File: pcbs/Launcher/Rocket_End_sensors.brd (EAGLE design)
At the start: 100 x 80 mm, 9 parts, among them U1 ARDUINO-MEGAPRO-5V, X1 22-23-2051, X3 22-23-2041, X5 22-23-2101, X6 22-23-2101, X7 22-23-2101, X8 22-23-2031

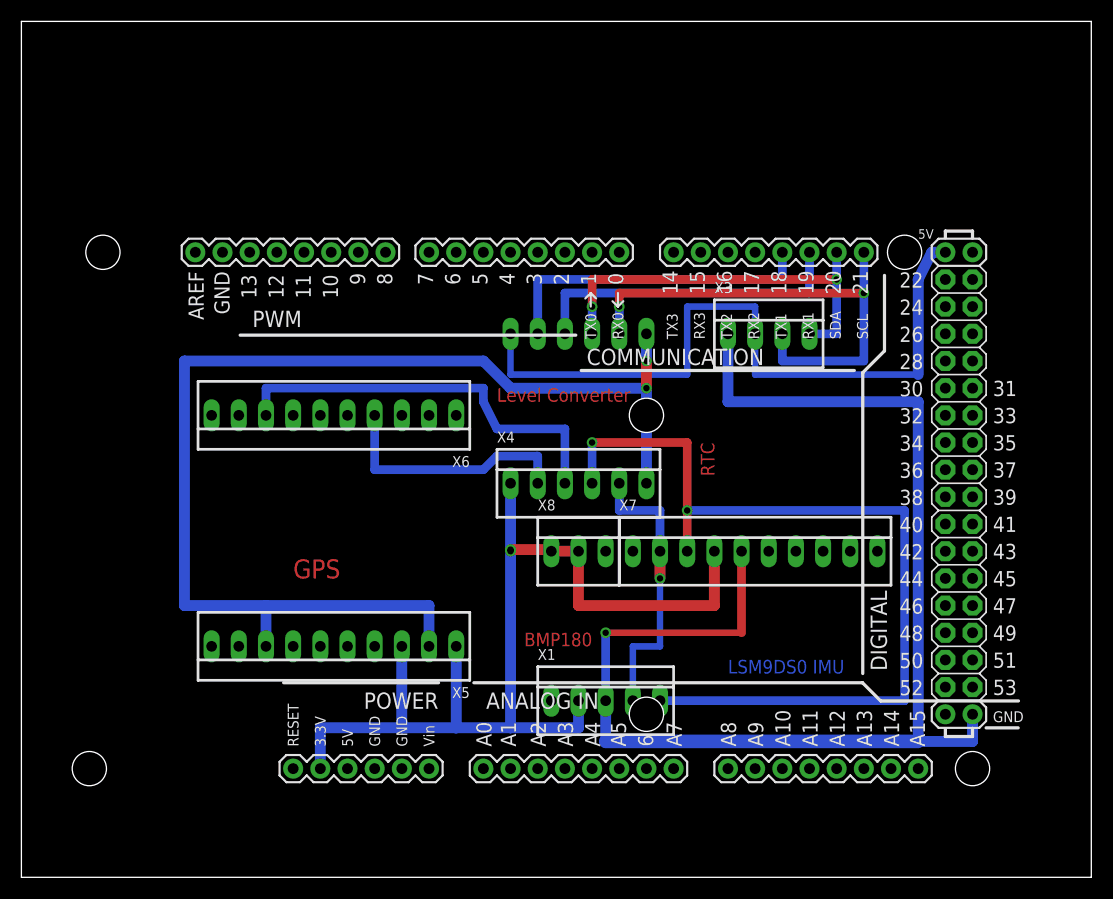
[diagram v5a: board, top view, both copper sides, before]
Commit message: * More space between tracks * Ground wire added to GPS module * Added extra holes, so we can do some hacks alter on the IMU
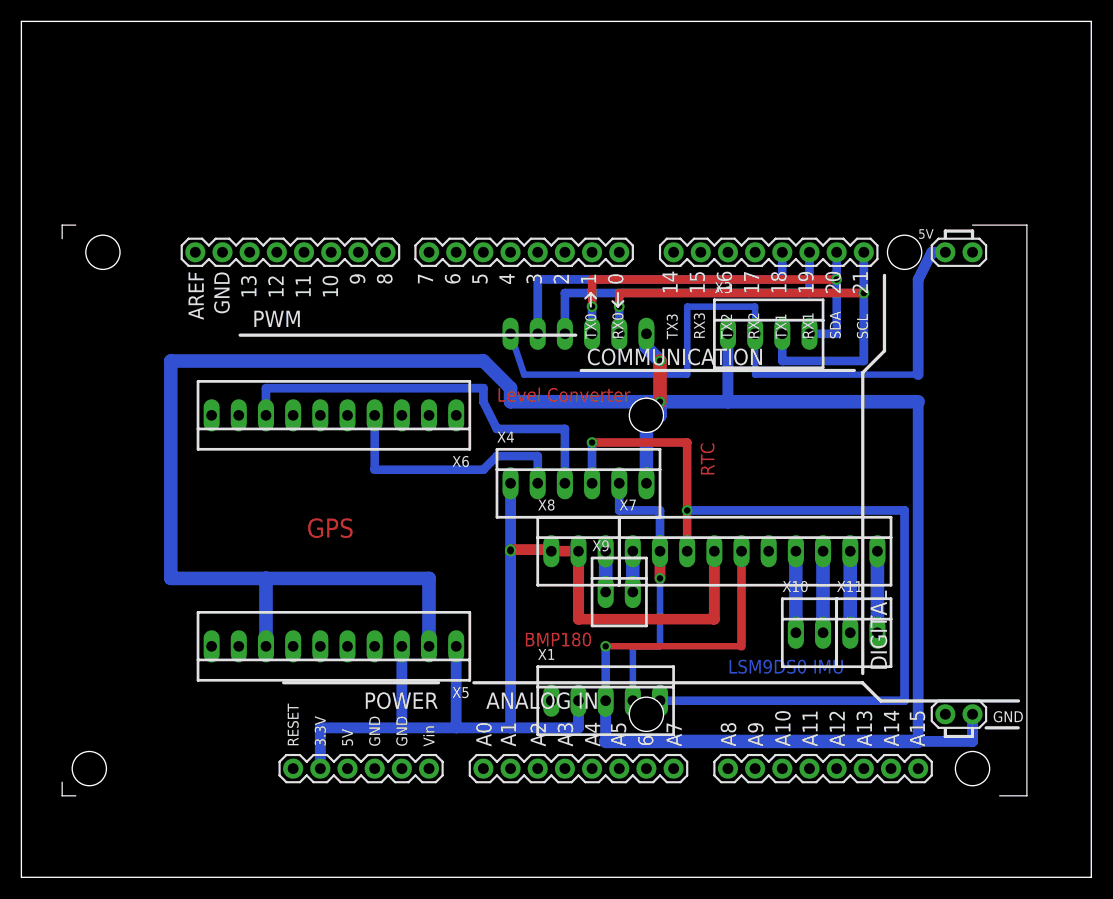
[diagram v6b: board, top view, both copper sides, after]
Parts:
- added X10, X11, X9: 22-23-2021, con-molex:22-23-2021
- U1: device SparkFun-Boards:ARDUINO_MEGA-PRO-5V -> JoeMega_Ether_Edited:ARDUINO_MEGA-PRO-5V
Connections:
- new net N$10: X10.1, X7.7
- new net N$11: X10.2, X7.8
- new net N$12: X11.1, X7.9
- new net N$13: X11.2, X7.10
- new net N$9: X7.1, X9.2
- net GND: now also X2.1, X4.6, X5.2, X5.8
- net N$7: now also X8.3, X9.1; no longer X2.1, X4.6, X5.2, X5.8
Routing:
- net GND: track 123.2 -> 248.5 mm, vias 1 -> 3
- net N$7: track 111.5 -> 3.81 mm, vias 2 -> 0
- net N$13: track 0.00 -> 7.62 mm
- net N$12: track 0.00 -> 7.62 mm
- net N$11: track 0.00 -> 7.62 mm
- net N$10: track 0.00 -> 7.62 mm
- net N$9: track 0.00 -> 3.81 mm
- net N$4: track 97.7 -> 100.2 mm
- net N$28: track 67.6 -> 66.5 mm
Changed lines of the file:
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@@
 <?xml version="1.0" encoding="utf-8"?>
 <!DOCTYPE eagle SYSTEM "eagle.dtd">
-<eagle version="7.1.0">
+<eagle version="7.3.0">
 <drawing>
 <settings>
@@
 <wire x1="0" y1="80" x2="0" y2="0" width="0" layer="20"/>
 <text x="63.5" y="40.64" size="1.27" layer="1" rot="R270">RTC</text>
-<text x="25.4" y="27.94" size="1.778" layer="1">GPS</text>
+<text x="26.67" y="31.75" size="1.778" layer="1">GPS</text>
 <text x="46.99" y="21.59" size="1.27" layer="1">BMP180</text>
 <text x="66.04" y="19.05" size="1.27" layer="16">LSM9DS0 IMU</text>
@@
 </autorouter>
 <elements>
-<element name="U1" library="SparkFun-Boards" package="ARDUINO_MEGA-PRO-5V" value="ARDUINO-MEGAPRO-5V" x="3.81" y="7.62"/>
+<element name="U1" library="JoeMega_Ether_Edited" package="ARDUINO_MEGA-PRO-5V" value="ARDUINO-MEGAPRO-5V" x="3.81" y="7.62"/>
 <element name="X3" library="con-molex" package="22-23-2041" value="22-23-2041" x="69.85" y="50.8">
 <attribute name="MF" value="MOLEX" x="69.85" y="50.8" size="1.778" layer="27" display="off"/>
@@
 <attribute name="MF" value="MOLEX" x="29.21" y="21.59" size="1.778" layer="27" rot="R180" display="off"/>
 <attribute name="OC_FARNELL" value="1756828" x="29.21" y="21.59" size="1.778" layer="27" rot="R180" display="off"/>
+</element>
+<element name="X9" library="con-molex" package="22-23-2021" value="22-23-2021" x="55.88" y="26.67">
+<attribute name="OC_FARNELL" value="1462926" x="55.88" y="26.67" size="1.778" layer="27" display="off"/>
+<attribute name="OC_NEWARK" value="25C3832" x="55.88" y="26.67" size="1.778" layer="27" display="off"/>
+<attribute name="MPN" value="22-23-2021" x="55.88" y="26.67" size="1.778" layer="27" display="off"/>
+<attribute name="MF" value="MOLEX" x="55.88" y="26.67" size="1.778" layer="27" display="off"/>
+</element>
+<element name="X10" library="con-molex" package="22-23-2021" value="22-23-2021" x="73.66" y="22.86">
+<attribute name="OC_FARNELL" value="1462926" x="73.66" y="22.86" size="1.778" layer="27" display="off"/>
+<attribute name="OC_NEWARK" value="25C3832" x="73.66" y="22.86" size="1.778" layer="27" display="off"/>
+<attribute name="MPN" value="22-23-2021" x="73.66" y="22.86" size="1.778" layer="27" display="off"/>
+<attribute name="MF" value="MOLEX" x="73.66" y="22.86" size="1.778" layer="27" display="off"/>
+</element>
+<element name="X11" library="con-molex" package="22-23-2021" value="22-23-2021" x="78.74" y="22.86">
+<attribute name="OC_FARNELL" value="1462926" x="78.74" y="22.86" size="1.778" layer="27" display="off"/>
+<attribute name="OC_NEWARK" value="25C3832" x="78.74" y="22.86" size="1.778" layer="27" display="off"/>
+<attribute name="MPN" value="22-23-2021" x="78.74" y="22.86" size="1.778" layer="27" display="off"/>
+<attribute name="MF" value="MOLEX" x="78.74" y="22.86" size="1.778" layer="27" display="off"/>
 </element>
 </elements>
@@
 <wire x1="68.58" y1="53.34" x2="62.23" y2="53.34" width="0.6096" layer="16"/>
 <wire x1="62.23" y1="53.34" x2="62.23" y2="46.99" width="0.6096" layer="16"/>
-<wire x1="62.23" y1="46.99" x2="45.72" y2="46.99" width="0.6096" layer="16"/>
-<wire x1="45.72" y1="46.99" x2="45.72" y2="50.8" width="0.6096" layer="16"/>
+<wire x1="62.23" y1="46.99" x2="46.99" y2="46.99" width="0.6096" layer="16"/>
+<wire x1="46.99" y1="46.99" x2="45.72" y2="50.8" width="0.6096" layer="16"/>
 </signal>
 <signal name="N$32">
@@
 <contactref element="U1" pad="GND@3"/>
 <wire x1="66.04" y1="50.8" x2="66.04" y2="44.45" width="1.016" layer="16"/>
-<wire x1="66.04" y1="44.45" x2="83.82" y2="44.45" width="1.016" layer="16"/>
+<wire x1="66.04" y1="44.45" x2="83.82" y2="44.45" width="1.27" layer="16"/>
 <wire x1="83.82" y1="44.45" x2="83.82" y2="12.7" width="1.016" layer="16"/>
 <wire x1="83.82" y1="12.7" x2="88.9" y2="12.7" width="1.016" layer="16"/>
@@
 <wire x1="54.61" y1="12.7" x2="83.82" y2="12.7" width="1.27" layer="16"/>
 <contactref element="X7" pad="5"/>
-<wire x1="67.31" y1="30.48" x2="67.31" y2="22.86" width="0.8128" layer="1"/>
-<wire x1="67.31" y1="22.86" x2="54.61" y2="22.86" width="0.6096" layer="1"/>
-<wire x1="54.61" y1="22.86" x2="54.61" y2="16.51" width="0.8128" layer="16"/>
-<via x="54.61" y="22.86" extent="1-16" drill="0.6" shape="square"/>
+<wire x1="67.31" y1="30.48" x2="67.31" y2="21.59" width="0.8128" layer="1"/>
+<wire x1="67.31" y1="21.59" x2="54.61" y2="21.59" width="0.6096" layer="1"/>
+<wire x1="54.61" y1="21.59" x2="54.61" y2="16.51" width="0.8128" layer="16"/>
+<via x="54.61" y="21.59" extent="1-16" drill="0.6" shape="square"/>
+<contactref element="X2" pad="1"/>
+<contactref element="X5" pad="2"/>
+<contactref element="X4" pad="6"/>
+<contactref element="X5" pad="8"/>
+<wire x1="38.1" y1="21.59" x2="38.1" y2="27.94" width="1.27" layer="16"/>
+<wire x1="38.1" y1="27.94" x2="22.86" y2="27.94" width="1.27" layer="16"/>
+<wire x1="22.86" y1="27.94" x2="22.86" y2="21.59" width="1.27" layer="16"/>
+<wire x1="66.04" y1="44.45" x2="59.69" y2="44.45" width="1.27" layer="16"/>
+<wire x1="59.69" y1="44.45" x2="45.72" y2="44.45" width="1.27" layer="16"/>
+<wire x1="45.72" y1="44.45" x2="45.72" y2="45.72" width="1.27" layer="16"/>
+<wire x1="45.72" y1="45.72" x2="43.18" y2="48.26" width="1.27" layer="16"/>
+<wire x1="43.18" y1="48.26" x2="13.97" y2="48.26" width="1.27" layer="16"/>
+<wire x1="13.97" y1="48.26" x2="13.97" y2="27.94" width="1.27" layer="16"/>
+<wire x1="13.97" y1="27.94" x2="22.86" y2="27.94" width="1.27" layer="16"/>
+<wire x1="58.42" y1="50.8" x2="58.42" y2="49.53" width="1.27" layer="16"/>
+<wire x1="58.42" y1="49.53" x2="59.69" y2="48.26" width="1.27" layer="16"/>
+<wire x1="59.69" y1="48.26" x2="59.69" y2="44.45" width="1.27" layer="1"/>
+<wire x1="59.69" y1="44.45" x2="59.69" y2="43.18" width="1.27" layer="16"/>
+<wire x1="59.69" y1="43.18" x2="58.42" y2="41.91" width="1.27" layer="16"/>
+<wire x1="58.42" y1="41.91" x2="58.42" y2="38.1" width="1.27" layer="16"/>
+<wire x1="58.42" y1="38.1" x2="58.42" y2="36.83" width="0" layer="19" extent="1-16"/>
+<via x="59.69" y="48.26" extent="1-16" drill="0.6" shape="square"/>
+<via x="59.69" y="44.45" extent="1-16" drill="0.6" shape="square"/>
 </signal>
 <signal name="N$1">
@@
 <wire x1="52.07" y1="30.48" x2="49.53" y2="30.48" width="1.016" layer="1"/>
 <via x="45.72" y="30.48" extent="1-16" drill="0.6" shape="square"/>
-<wire x1="64.77" y1="30.48" x2="64.77" y2="25.4" width="1.016" layer="1"/>
-<wire x1="64.77" y1="25.4" x2="52.07" y2="25.4" width="1.016" layer="1"/>
-<wire x1="52.07" y1="25.4" x2="52.07" y2="30.48" width="1.016" layer="1"/>
+<wire x1="64.77" y1="30.48" x2="64.77" y2="24.13" width="1.016" layer="1"/>
+<wire x1="64.77" y1="24.13" x2="52.07" y2="24.13" width="1.016" layer="1"/>
+<wire x1="52.07" y1="24.13" x2="52.07" y2="30.48" width="1.016" layer="1"/>
 <via x="45.72" y="30.6324" extent="1-16" drill="0.6" shape="square"/>
 <contactref element="X5" pad="1"/>
@@
 </signal>
 <signal name="N$7">
-<contactref element="X4" pad="6"/>
-<contactref element="X2" pad="1"/>
-<wire x1="58.42" y1="50.8" x2="58.42" y2="48.26" width="1.016" layer="16"/>
-<wire x1="58.42" y1="48.26" x2="58.42" y2="45.72" width="1.016" layer="1"/>
-<wire x1="58.42" y1="45.72" x2="58.42" y2="36.83" width="1.016" layer="16"/>
-<via x="58.42" y="45.72" extent="1-16" drill="0.6" shape="square"/>
-<via x="58.42" y="48.26" extent="1-16" drill="0.6" shape="square"/>
-<wire x1="22.86" y1="25.4" x2="38.1" y2="25.4" width="1.016" layer="16"/>
-<wire x1="22.86" y1="25.4" x2="15.24" y2="25.4" width="1.016" layer="16"/>
-<wire x1="15.24" y1="25.4" x2="15.24" y2="48.26" width="1.016" layer="16"/>
-<wire x1="15.24" y1="48.26" x2="43.18" y2="48.26" width="1.016" layer="16"/>
-<wire x1="43.18" y1="48.26" x2="45.72" y2="45.72" width="1.016" layer="16"/>
-<wire x1="45.72" y1="45.72" x2="58.42" y2="45.72" width="1.016" layer="16"/>
-<contactref element="X5" pad="2"/>
-<contactref element="X5" pad="8"/>
-<wire x1="38.1" y1="21.59" x2="38.1" y2="25.4" width="1.016" layer="16"/>
-<wire x1="22.86" y1="21.59" x2="22.86" y2="25.4" width="1.016" layer="16"/>
+<contactref element="X8" pad="3"/>
+<contactref element="X9" pad="1"/>
+<wire x1="54.61" y1="30.48" x2="54.61" y2="26.67" width="1.27" layer="16"/>
+</signal>
+<signal name="N$9">
+<contactref element="X7" pad="1"/>
+<contactref element="X9" pad="2"/>
+<wire x1="57.15" y1="30.48" x2="57.15" y2="26.67" width="1.27" layer="16"/>
+</signal>
+<signal name="N$10">
+<contactref element="X7" pad="7"/>
+<contactref element="X10" pad="1"/>
+<wire x1="72.39" y1="22.86" x2="72.39" y2="30.48" width="1.27" layer="16"/>
+</signal>
+<signal name="N$11">
+<contactref element="X7" pad="8"/>
+<contactref element="X10" pad="2"/>
+<wire x1="74.93" y1="30.48" x2="74.93" y2="22.86" width="1.27" layer="16"/>
+</signal>
+<signal name="N$12">
+<contactref element="X7" pad="9"/>
+<contactref element="X11" pad="1"/>
+<wire x1="77.47" y1="30.48" x2="77.47" y2="22.86" width="1.27" layer="16"/>
+</signal>
+<signal name="N$13">
+<contactref element="X7" pad="10"/>
+<contactref element="X11" pad="2"/>
+<wire x1="80.01" y1="30.48" x2="80.01" y2="22.86" width="1.27" layer="16"/>
 </signal>
 </signals>

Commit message: * Fixed up board and library so that holes will not go through tracks, etc.
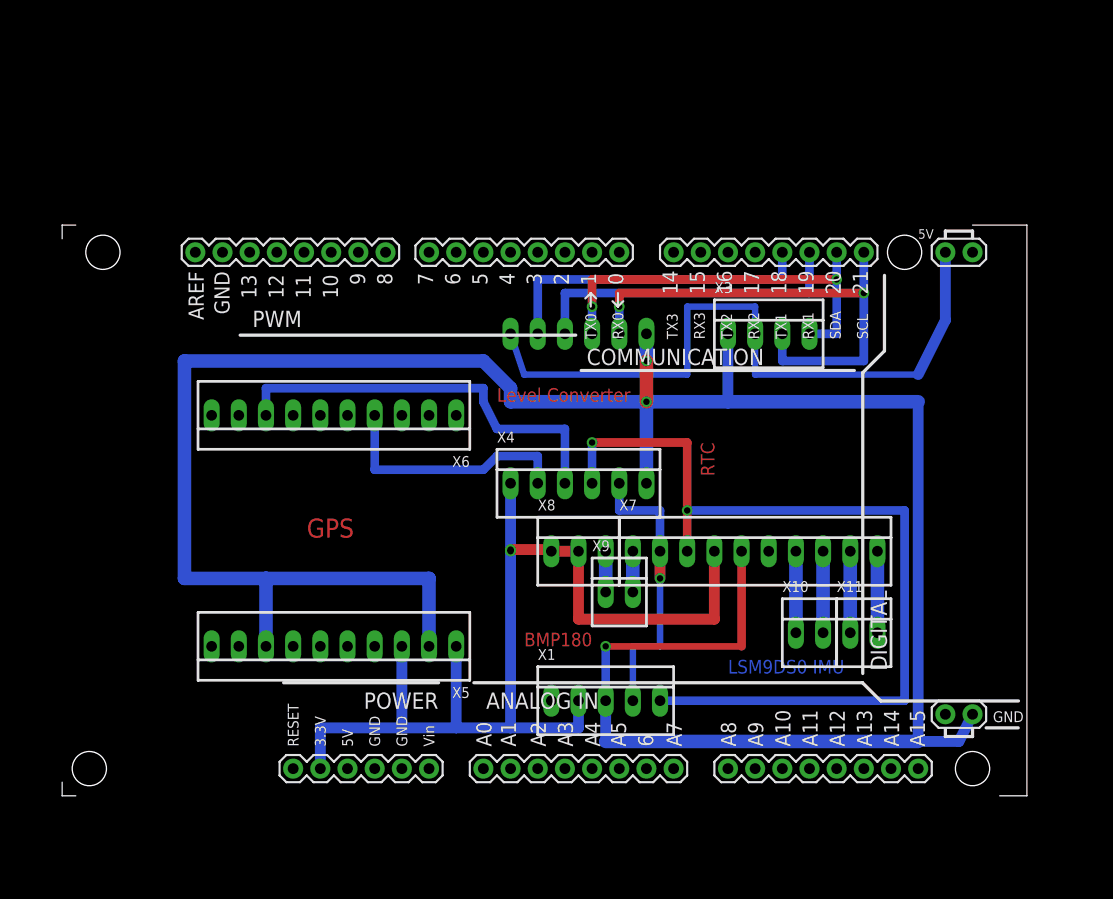
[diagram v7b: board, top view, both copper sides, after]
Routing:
- net GND: track 248.5 -> 243.9 mm
- net N$28: track 66.5 -> 65.6 mm
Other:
- board outline removed
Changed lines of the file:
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@@
 <board>
 <plain>
-<wire x1="0" y1="0" x2="100" y2="0" width="0" layer="20"/>
-<wire x1="100" y1="0" x2="100" y2="80" width="0" layer="20"/>
-<wire x1="100" y1="80" x2="0" y2="80" width="0" layer="20"/>
-<wire x1="0" y1="80" x2="0" y2="0" width="0" layer="20"/>
 <text x="63.5" y="40.64" size="1.27" layer="1" rot="R270">RTC</text>
 <text x="26.67" y="31.75" size="1.778" layer="1">GPS</text>
@@
 <wire x1="68.58" y1="50.8" x2="68.58" y2="46.99" width="0.6096" layer="16"/>
 <wire x1="68.58" y1="46.99" x2="83.82" y2="46.99" width="0.6096" layer="16"/>
-<wire x1="83.82" y1="46.99" x2="83.82" y2="55.88" width="1.016" layer="16"/>
-<wire x1="83.82" y1="55.88" x2="85.09" y2="58.42" width="1.016" layer="16"/>
-<wire x1="85.09" y1="58.42" x2="86.36" y2="58.42" width="1.016" layer="16"/>
+<wire x1="83.82" y1="46.99" x2="86.36" y2="52.07" width="1.016" layer="16"/>
+<wire x1="86.36" y1="52.07" x2="86.36" y2="58.42" width="1.016" layer="16"/>
 <contactref element="X2" pad="6"/>
 <wire x1="68.58" y1="50.8" x2="68.58" y2="53.34" width="0.6096" layer="16"/>
@@
 <wire x1="66.04" y1="44.45" x2="83.82" y2="44.45" width="1.27" layer="16"/>
 <wire x1="83.82" y1="44.45" x2="83.82" y2="12.7" width="1.016" layer="16"/>
-<wire x1="83.82" y1="12.7" x2="88.9" y2="12.7" width="1.016" layer="16"/>
-<wire x1="88.9" y1="12.7" x2="88.9" y2="15.24" width="1.016" layer="16"/>
+<wire x1="83.82" y1="12.7" x2="87.63" y2="12.7" width="1.016" layer="16"/>
+<wire x1="87.63" y1="12.7" x2="88.9" y2="15.24" width="1.016" layer="16"/>
 <contactref element="X1" pad="3"/>
 <wire x1="54.61" y1="16.51" x2="54.61" y2="12.7" width="1.016" layer="16"/>
@@
 <wire x1="38.1" y1="27.94" x2="22.86" y2="27.94" width="1.27" layer="16"/>
 <wire x1="22.86" y1="27.94" x2="22.86" y2="21.59" width="1.27" layer="16"/>
-<wire x1="66.04" y1="44.45" x2="59.69" y2="44.45" width="1.27" layer="16"/>
-<wire x1="59.69" y1="44.45" x2="45.72" y2="44.45" width="1.27" layer="16"/>
+<wire x1="66.04" y1="44.45" x2="58.42" y2="44.45" width="1.27" layer="16"/>
+<wire x1="58.42" y1="44.45" x2="45.72" y2="44.45" width="1.27" layer="16"/>
 <wire x1="45.72" y1="44.45" x2="45.72" y2="45.72" width="1.27" layer="16"/>
 <wire x1="45.72" y1="45.72" x2="43.18" y2="48.26" width="1.27" layer="16"/>
-<wire x1="43.18" y1="48.26" x2="13.97" y2="48.26" width="1.27" layer="16"/>
-<wire x1="13.97" y1="48.26" x2="13.97" y2="27.94" width="1.27" layer="16"/>
-<wire x1="13.97" y1="27.94" x2="22.86" y2="27.94" width="1.27" layer="16"/>
-<wire x1="58.42" y1="50.8" x2="58.42" y2="49.53" width="1.27" layer="16"/>
-<wire x1="58.42" y1="49.53" x2="59.69" y2="48.26" width="1.27" layer="16"/>
-<wire x1="59.69" y1="48.26" x2="59.69" y2="44.45" width="1.27" layer="1"/>
-<wire x1="59.69" y1="44.45" x2="59.69" y2="43.18" width="1.27" layer="16"/>
-<wire x1="59.69" y1="43.18" x2="58.42" y2="41.91" width="1.27" layer="16"/>
-<wire x1="58.42" y1="41.91" x2="58.42" y2="38.1" width="1.27" layer="16"/>
-<wire x1="58.42" y1="38.1" x2="58.42" y2="36.83" width="0" layer="19" extent="1-16"/>
-<via x="59.69" y="48.26" extent="1-16" drill="0.6" shape="square"/>
-<via x="59.69" y="44.45" extent="1-16" drill="0.6" shape="square"/>
+<wire x1="43.18" y1="48.26" x2="15.24" y2="48.26" width="1.27" layer="16"/>
+<wire x1="15.24" y1="48.26" x2="15.24" y2="27.94" width="1.27" layer="16"/>
+<wire x1="15.24" y1="27.94" x2="22.86" y2="27.94" width="1.27" layer="16"/>
+<wire x1="58.42" y1="50.8" x2="58.42" y2="48.26" width="1.27" layer="16"/>
+<wire x1="58.42" y1="48.26" x2="58.42" y2="44.45" width="1.27" layer="1"/>
+<wire x1="58.42" y1="44.45" x2="58.42" y2="38.1" width="1.27" layer="16"/>
+<via x="58.42" y="48.26" extent="1-16" drill="0.6" shape="square"/>
+<via x="58.42" y="44.45" extent="1-16" drill="0.6" shape="square"/>
+<wire x1="58.42" y1="38.1" x2="58.42" y2="36.83" width="0" layer="19" extent="16-16"/>
 </signal>
 <signal name="N$1">
